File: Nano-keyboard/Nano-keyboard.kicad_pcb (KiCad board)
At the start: 2 copper layers, 120.1 x 80.2 mm, 39 parts, among them U1 QBC847BL, U2 ESP32-WROOM-32, U3 QBC847BL, U4 QBC847BL, U5 EN12-HN22AF25, U6 EN12-HN22AF25, U7 TP4050

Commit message: Minor changes
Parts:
- removed LED1, LED10, LED2, LED3, LED4, LED5, LED6, LED7, LED8, LED9: LRTBGVSR-U4V2-JW+A6BB-D8+S2U2-7Z-20-S, lib:LRTBGVSRU4V2JWA6BBD8S2U27Z20S
- removed U1, U3, U4: QBC847BL, lib:SOT96P237X111-3N
- D1, D10, D2, D3, D4, D5, D6, D7, D8, D9: footprint Diode_THT:D_DO-35_SOD27_P3.81mm_Vertical_AnodeUp -> Diode_THT:D_DO-35_SOD27_P7.62mm_Horizontal
- moved LED0 51.7 mm to (109.2, 69.8), turned to 90 degrees
- moved D1 3.83 mm to (106.9, 135.9)
- moved D2 3.83 mm to (124.9, 135.9)
- moved D3 3.83 mm to (142.9, 135.9)
- moved D4 3.83 mm to (160.8, 135.9)
- moved B0 3.83 mm to (98.7, 120.7)
- moved B1 3.83 mm to (117.7, 120.7)
- moved B2 3.83 mm to (135.7, 120.7)
- moved B3 3.83 mm to (153.7, 120.7)
- moved B4 3.83 mm to (171.6, 120.7)
- moved B6 1.91 mm to (135.5, 99.7)
- moved D5 1.91 mm to (106.7, 115.1)
- moved D6 1.91 mm to (124.4, 115.1)
- moved D7 1.91 mm to (142.7, 115.1)
- moved D8 1.91 mm to (160.9, 115.1)
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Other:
- board size 120.1 x 80.2 mm -> 113.3 x 77.2 mm

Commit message: Initial routing
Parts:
- removed U7: TP4050, lib:TP4050-module
- added U1: AMS1117, Package_TO_SOT_SMD:SOT-223-3_TabPin2, F.Cu at (72.4, 95.2)
- added U3: J5019, lib:J5019-module, F.Cu at (90.7, 100.4)
- moved B2 5.45 mm to (140.8, 118.7)
- moved B3 5.45 mm to (158.8, 118.7)
- moved B4 5.45 mm to (176.7, 118.7)
- moved B7 5.45 mm to (158.7, 97.8)
- moved B9 5.45 mm to (140.6, 76.8)
- moved B6 5.45 mm to (140.6, 97.8)
- moved D8 5.45 mm to (166.0, 113.2)
- moved B0 5.45 mm to (103.8, 118.7)
- moved B1 5.45 mm to (122.8, 118.7)
- moved B5 5.45 mm to (122.6, 97.8)
- moved D1 5.45 mm to (112.0, 134.0)
- moved U5 5.45 mm to (122.1, 75.2)
- moved B10 5.45 mm to (158.7, 76.8)
- moved B8 5.45 mm to (176.8, 97.8)
- moved D10 5.45 mm to (147.9, 92.1)
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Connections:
- LED0 pad A1: /ANODE_G -> /LED_GREEN
- LED0 pad A2: /ANODE_R -> /LED_RED
- LED0 pad A3: /ANODE_B -> /LED_BLUE
- U2 pad 16: unconnected-(U2-Pad16) -> ROW1
- U2 pad 23: unconnected-(U2-Pad23) -> ROW2
- U2 pad 24: unconnected-(U2-Pad24) -> ROW3
- U2 pad 30: unconnected-(U2-Pad30) -> /FUNC
- U2 pad 31: unconnected-(U2-Pad31) -> COL1
- U2 pad 33: unconnected-(U2-Pad33) -> COL2
- U2 pad 36: unconnected-(U2-Pad36) -> COL3
- U2 pad 37: unconnected-(U2-Pad37) -> COL4
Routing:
- net ROW1: track 0.00 -> 128.3 mm
- net COL4: track 0.00 -> 105.2 mm
- net COL2: track 0.00 -> 96.2 mm
- net ROW2: track 0.00 -> 92.3 mm
- net COL3: track 0.00 -> 86.6 mm
- net COL1: track 0.00 -> 79.3 mm
- net /FUNC: track 0.00 -> 45.7 mm, vias 0 -> 1
- net ROW3: track 0.00 -> 36.4 mm, vias 0 -> 2
- net Net-(B6-Pad1): track 0.00 -> 16.8 mm
- net Net-(B7-Pad1): track 0.00 -> 16.8 mm
- net Net-(B9-Pad1): track 0.00 -> 16.7 mm
- net Net-(B5-Pad1): track 0.00 -> 16.7 mm
- net Net-(B8-Pad1): track 0.00 -> 16.7 mm
- net Net-(B10-Pad1): track 0.00 -> 16.6 mm
- net Net-(B4-Pad1): track 0.00 -> 16.6 mm
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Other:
- board size 113.3 x 77.2 mm -> 118.3 x 77.2 mm

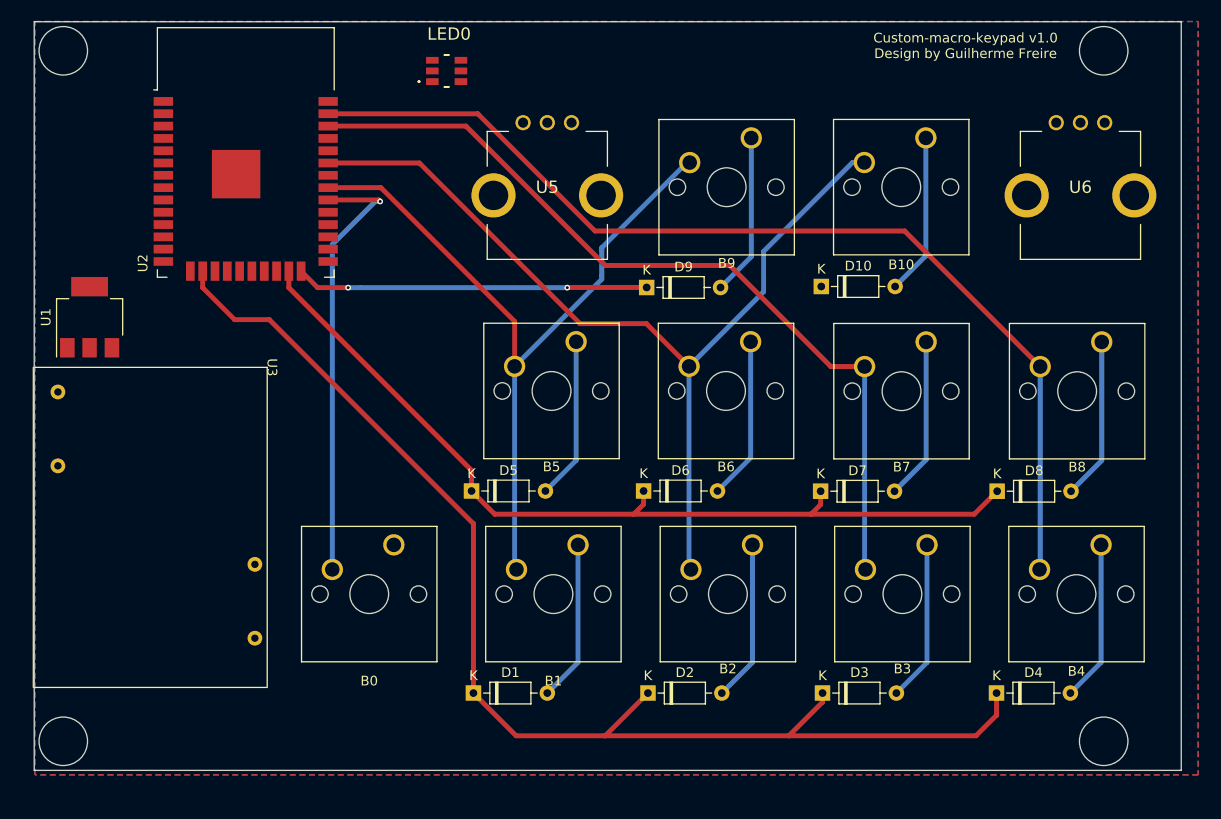
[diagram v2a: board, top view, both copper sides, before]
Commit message: Added Resistors and Capacitor
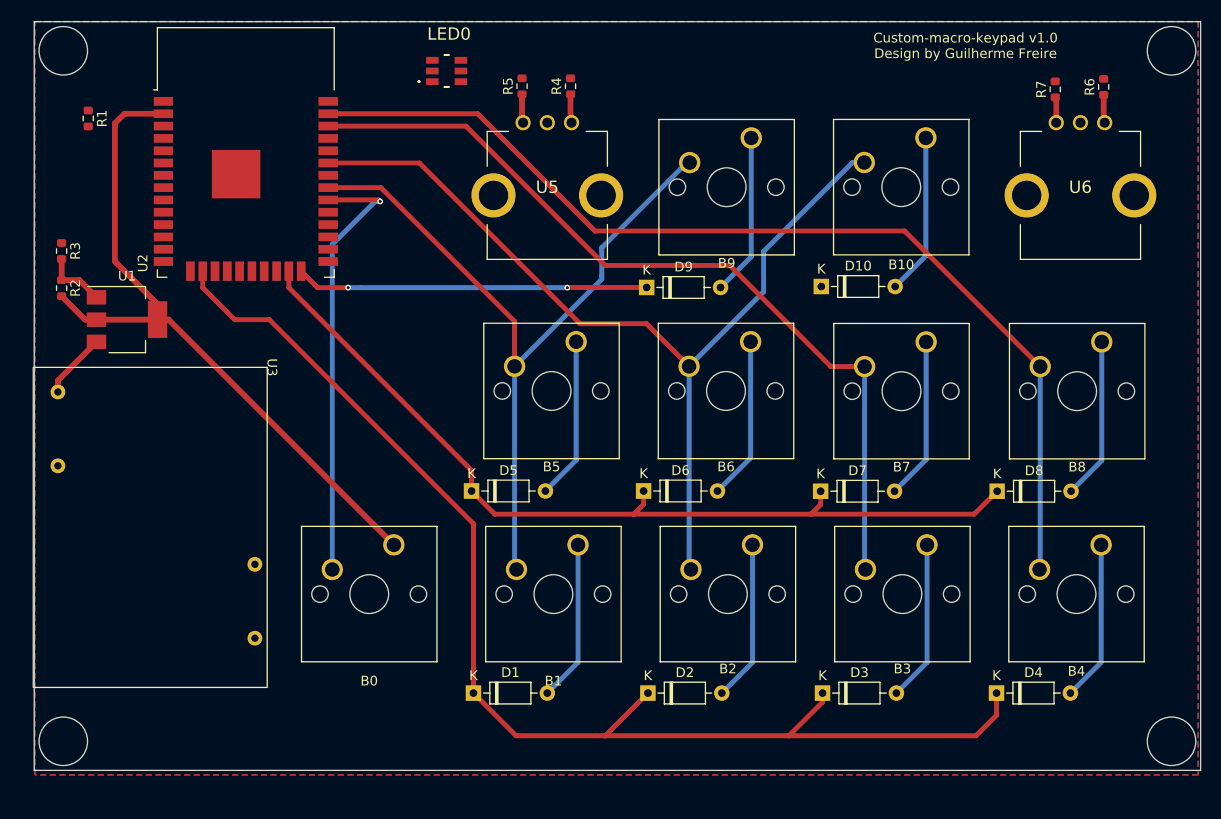
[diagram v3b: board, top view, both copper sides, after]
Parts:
- added R1: R_0603, lib:R_0603_1608Metric, F.Cu at (72.2, 74.8)
- added R2: 600R, lib:R_0603_1608Metric, F.Cu at (69.5, 92.2)
- added R3: 1kR, lib:R_0603_1608Metric, F.Cu at (69.5, 88.4)
- added R4: R_0603, lib:R_0603_1608Metric, F.Cu at (122.0, 71.4)
- added R5: R_0603, lib:R_0603_1608Metric, F.Cu at (117.0, 71.4)
- added R6: R_0603, lib:R_0603_1608Metric, F.Cu at (177.0, 71.5)
- added R7: R_0603, lib:R_0603_1608Metric, F.Cu at (172.0, 71.8)
- moved U1 3.87 mm to (76.2, 95.5), turned to 0 degrees
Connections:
- U1 pad 1: unconnected-(U1-Pad1) -> Net-(U1-Pad1)
- U2 pad 11: unconnected-(U2-Pad11) -> /ENCODER1_A
- U2 pad 12: unconnected-(U2-Pad12) -> /ENCODER1_B
- U2 pad 13: unconnected-(U2-Pad13) -> /ENCODER2_A
- U2 pad 14: unconnected-(U2-Pad14) -> /ENCODER2_B
- U2 pad 3: unconnected-(U2-Pad3) -> /ESP_EN
- U5 pad A1: unconnected-(U5-PadA1) -> /ENCODER2_A
- U5 pad B1: unconnected-(U5-PadB1) -> /ENCODER2_B
- U5 pad C1: Net-(U5-PadC1) -> GND
- U6 pad A1: unconnected-(U6-PadA1) -> /ENCODER1_A
- U6 pad B1: unconnected-(U6-PadB1) -> /ENCODER1_B
- U6 pad C1: Net-(U5-PadC1) -> GND
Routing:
- net +3V3: track 0.00 -> 72.6 mm
- net Net-(U1-Pad3): track 0.00 -> 6.81 mm
- net Net-(U1-Pad1): track 0.00 -> 6.51 mm
- net /ENCODER2_B: track 0.00 -> 2.98 mm
- net /ENCODER2_A: track 0.00 -> 2.98 mm
- net /ENCODER1_A: track 0.00 -> 2.90 mm
- net /ENCODER1_B: track 0.00 -> 2.65 mm
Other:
- board size 118.3 x 77.2 mm -> 120.3 x 77.2 mm

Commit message: Routing changes
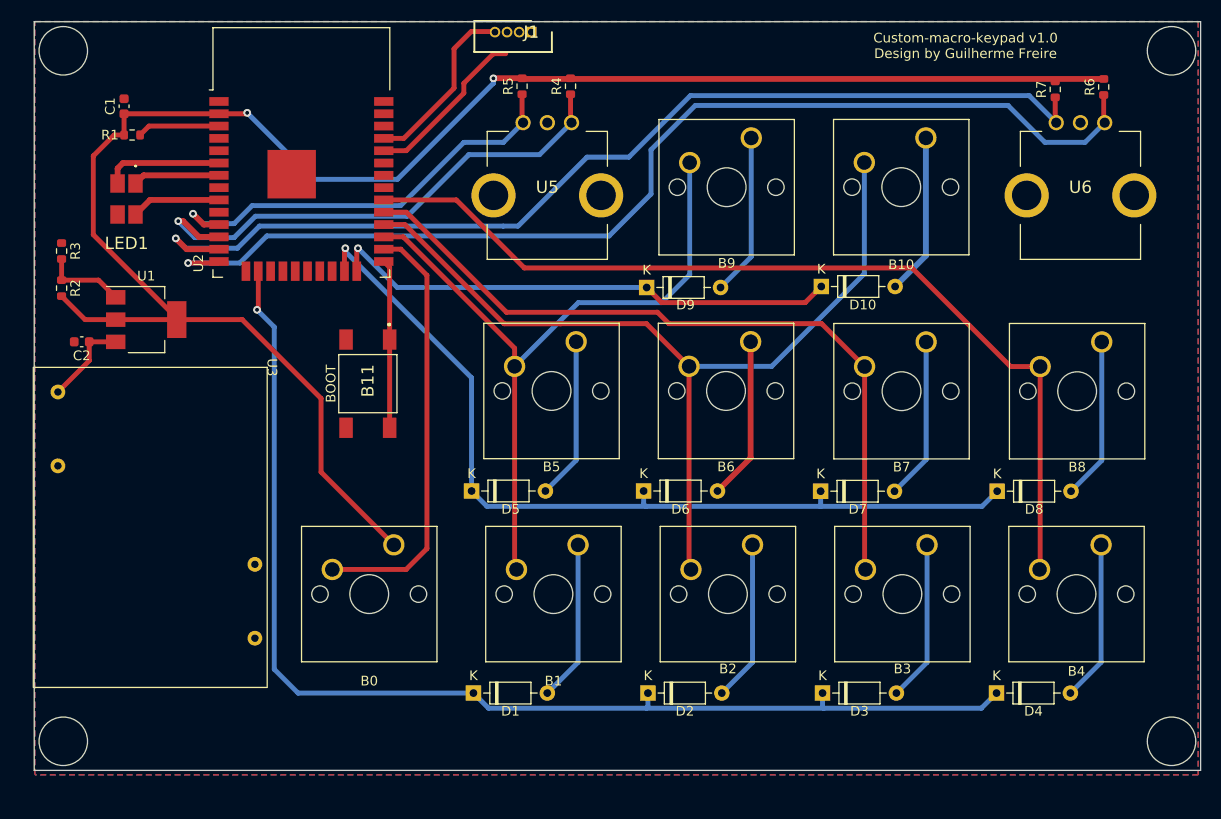
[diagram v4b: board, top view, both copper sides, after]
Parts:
- removed LED0: LRTBGVSR-U4V2-JW+A6BB-D8+S2U2-7Z-20-S, lib:LRTBGVSRU4V2JWA6BBD8S2U27Z20S
- added B11: LL3301NF065QG, lib:LL3301NF065QG, F.Cu at (101.1, 102.1)
- added C1: C_0603, lib:C_0603_1608Metric, F.Cu at (75.9, 73.5)
- added C2: C_0603, lib:C_0603_1608Metric, F.Cu at (71.6, 97.8)
- added J1: 125SH-B-04-TS, lib:SHDR4W35P0X125_1X4_800X320X420P, F.Cu at (118.0, 65.8)
- added LED1: 598-8610-307F, lib:5988610307F, F.Cu at (76.2, 83.1)
- R2: value 600R -> R_0603
- R3: value 1kR -> R_0603
- moved U2 5.73 mm to (94.2, 81.2)
- moved R1 4.83 mm to (76.8, 76.5), turned to 0 degrees
- moved U1 1.98 mm to (78.2, 95.5)
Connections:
- U2 pad 11: /ENCODER1_A -> /ENCODER2_B
- U2 pad 12: /ENCODER1_B -> /ENCODER2_A
- U2 pad 13: /ENCODER2_A -> /ENCODER1_B
- U2 pad 14: /ENCODER2_B -> /ENCODER1_A
- U2 pad 26: unconnected-(U2-Pad26) -> /FUNC
- U2 pad 27: unconnected-(U2-Pad27) -> COL1
- U2 pad 28: unconnected-(U2-Pad28) -> COL2
- U2 pad 29: unconnected-(U2-Pad29) -> COL3
- U2 pad 30: /FUNC -> COL4
- U2 pad 31: COL1 -> unconnected-(U2-Pad31)
- U2 pad 33: COL2 -> unconnected-(U2-Pad33)
- U2 pad 34: unconnected-(U2-Pad34) -> /RX0
- U2 pad 35: unconnected-(U2-Pad35) -> /TX0
- U2 pad 36: COL3 -> unconnected-(U2-Pad36)
- U2 pad 37: COL4 -> unconnected-(U2-Pad37)
- U2 pad 6: /LED_GREEN -> /LED_BLUE
- U2 pad 7: /LED_BLUE -> /LED_GREEN
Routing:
- net +3V3: track 72.6 -> 184.6 mm, vias 0 -> 2
- net /ENCODER1_A: track 2.90 -> 112.5 mm, vias 0 -> 1
- net /ENCODER1_B: track 2.65 -> 106.5 mm, vias 0 -> 1
- net /ENCODER2_A: track 2.98 -> 54.0 mm, vias 0 -> 1
- net /ENCODER2_B: track 2.98 -> 44.9 mm, vias 0 -> 1
- net /TX0: track 0.00 -> 18.5 mm
- net /BOOT: track 0.00 -> 17.4 mm
- net /RX0: track 0.00 -> 17.3 mm
- net ROW3: track 36.4 -> 53.2 mm, vias 2 -> 1
- net /LED_BLUE: track 0.00 -> 12.2 mm
- net COL4: track 105.2 -> 95.8 mm
- net COL3: track 86.6 -> 77.2 mm
- net /LED_RED: track 0.00 -> 9.23 mm
- net /LED_GREEN: track 0.00 -> 8.96 mm
- net /ESP_EN: track 0.00 -> 8.52 mm
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
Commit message: Routing Done [Pending Revision]
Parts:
- added J2: 125SH-B-02-TS, lib:125SHB02TS, F.Cu at (80.5, 140.1)
- added R8: R_0603, lib:R_0603_1608Metric, F.Cu at (76.1, 88.1)
- moved J1 0.99 mm to (117.1, 66.4)
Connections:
- LED1 pad 4: GND -> Net-(LED1-Pad4)
- U3 pad 1: unconnected-(U3-Pad1) -> Net-(U3-Pad1)
- U3 pad 2: unconnected-(U3-Pad2) -> Net-(U3-Pad2)
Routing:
- net Net-(U3-Pad1): track 0.00 -> 25.5 mm
- net Net-(U3-Pad2): track 0.00 -> 16.7 mm
- net Net-(LED1-Pad4): track 0.00 -> 3.41 mm
- net /TX0: track 18.5 -> 17.3 mm
- net /RX0: track 17.3 -> 18.0 mm
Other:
- board text added: "Nano-Keyboard v1.1 Design by Guilherme Freire"
- board text removed: "Custom-macro-keypad v1.0 Design by Guilherme Freire"

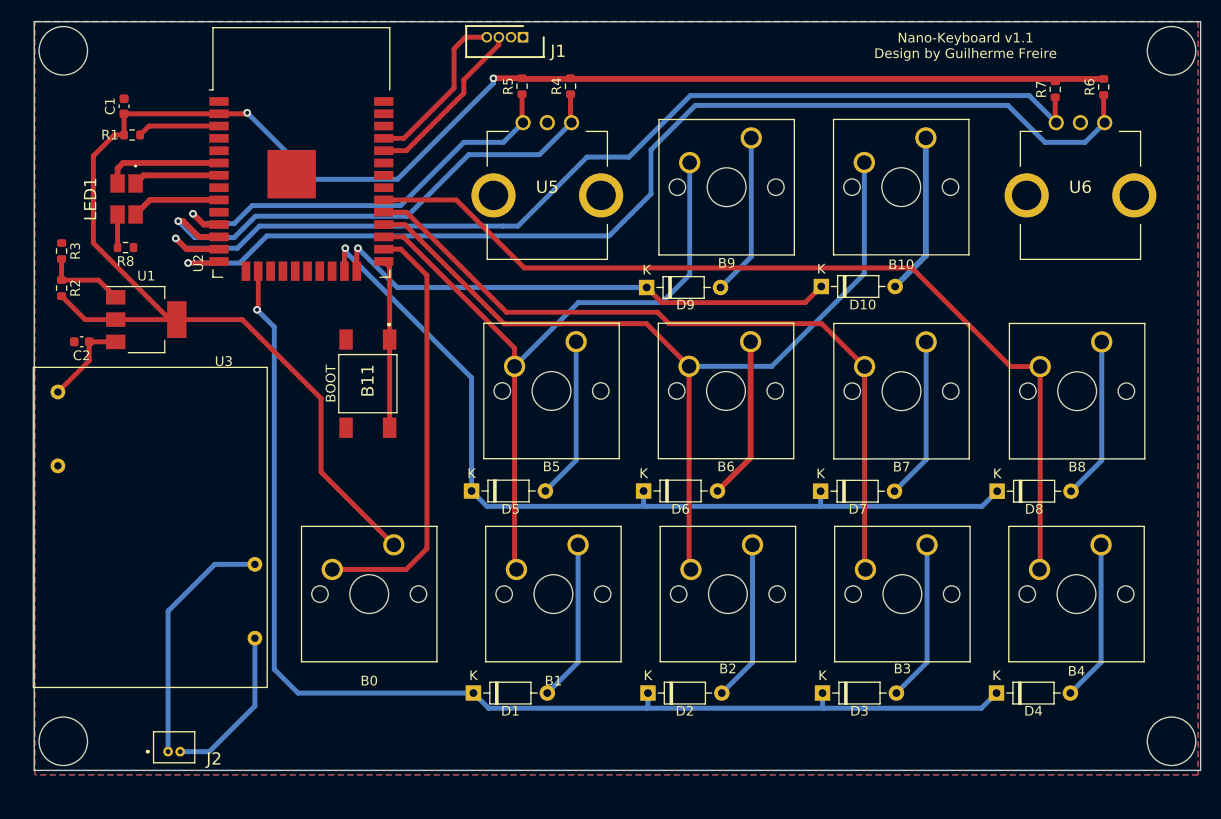
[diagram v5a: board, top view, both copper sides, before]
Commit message: Added RGB leds
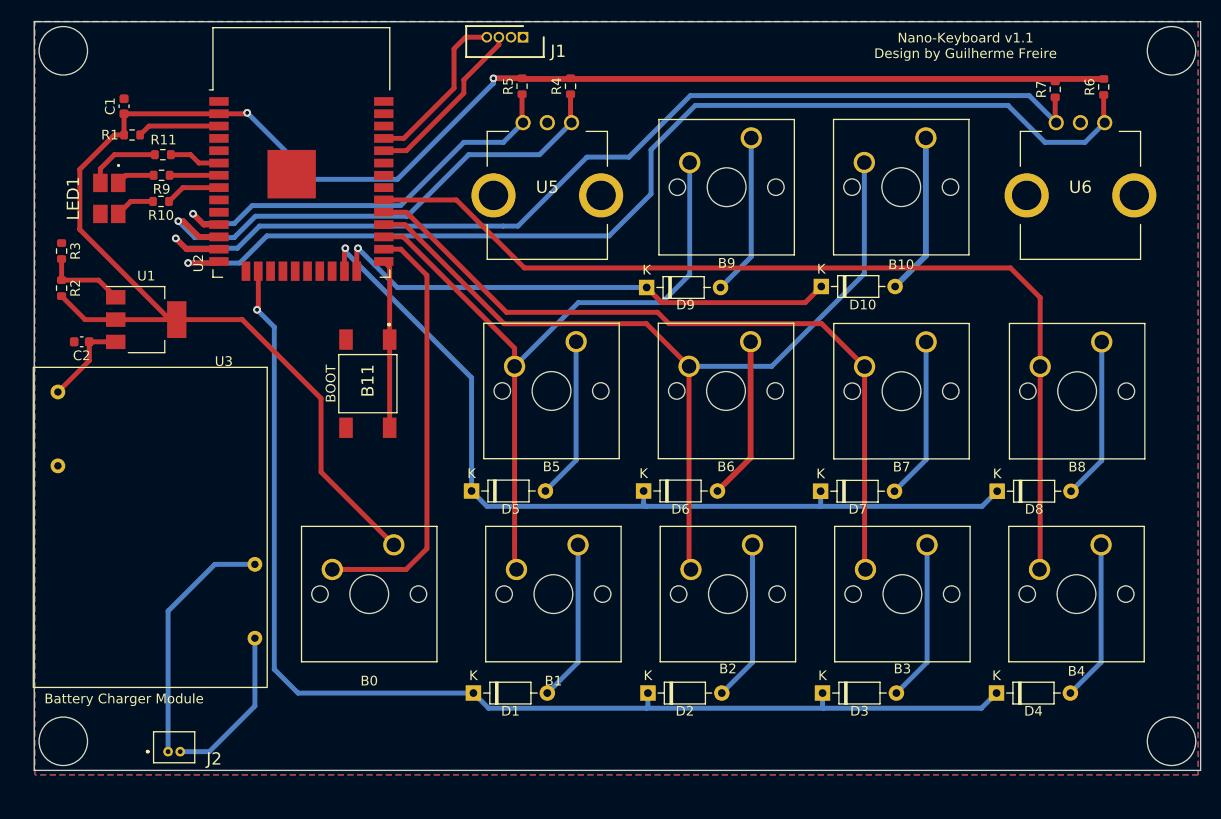
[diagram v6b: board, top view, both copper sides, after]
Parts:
- removed R8: R_0603, lib:R_0603_1608Metric
- added R10: R_0603, lib:R_0603_1608Metric, F.Cu at (79.8, 83.3)
- added R11: R_0603, lib:R_0603_1608Metric, F.Cu at (79.9, 78.5)
- added R9: R_0603, lib:R_0603_1608Metric, F.Cu at (79.8, 80.6)
- moved LED1 1.78 mm to (74.4, 83.0)
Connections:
- LED1 pad 1: /LED_GREEN -> Net-(LED1-Pad1)
- LED1 pad 2: /LED_RED -> Net-(LED1-Pad2)
- LED1 pad 3: /LED_BLUE -> Net-(LED1-Pad3)
- LED1 pad 4: Net-(LED1-Pad4) -> GND
- U2 pad 8: unconnected-(U2-Pad8) -> /LED_RED
- U2 pad 9: /LED_RED -> unconnected-(U2-Pad9)
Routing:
- net Net-(LED1-Pad3): track 0.00 -> 7.69 mm
- net /LED_BLUE: track 12.2 -> 5.32 mm
- net COL4: track 95.8 -> 100.0 mm
- net Net-(LED1-Pad2): track 0.00 -> 4.12 mm
- net Net-(LED1-Pad1): track 0.00 -> 3.97 mm
- net /LED_GREEN: track 8.96 -> 5.09 mm
- net /LED_RED: track 9.23 -> 5.74 mm
- net Net-(LED1-Pad4): track 3.41 -> 0.00 mm
- net +3V3: track 185.1 -> 186.2 mm
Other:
- board text added: "Battery Charger Module"

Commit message: Board Dimensions changes
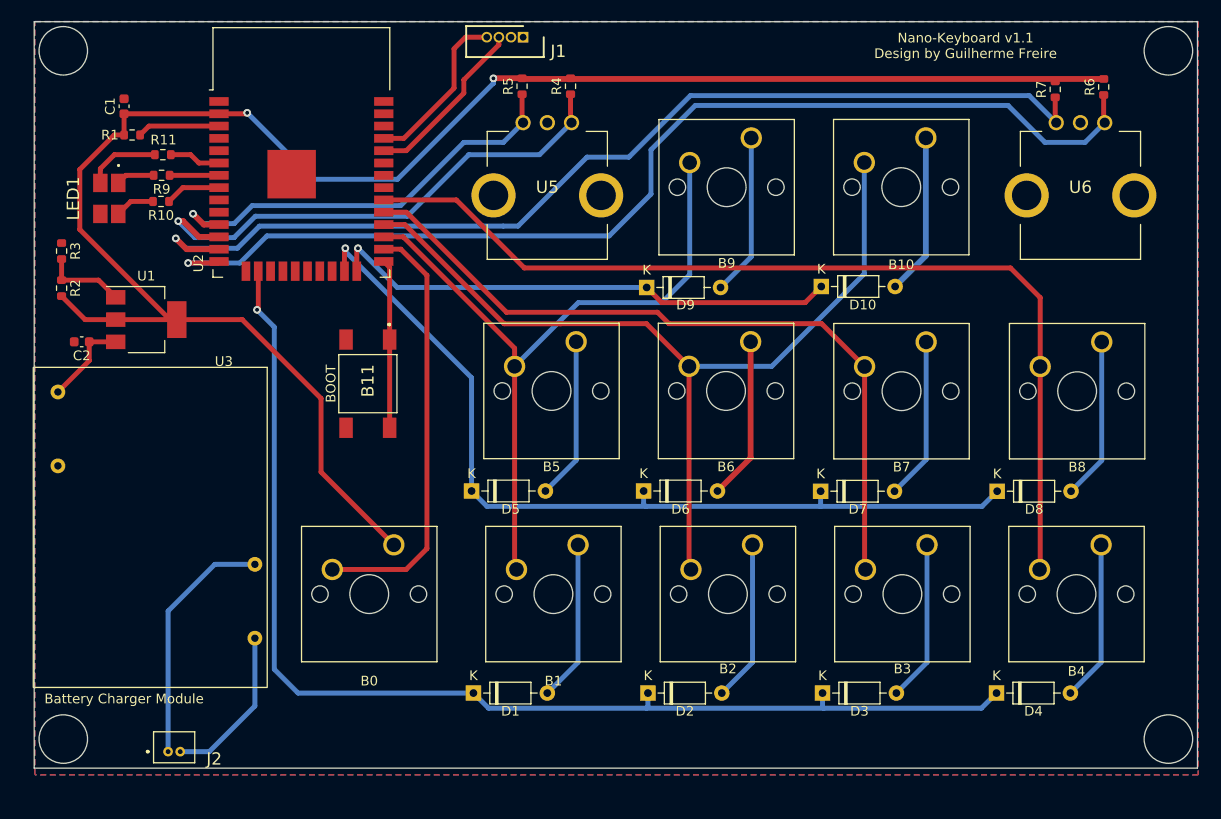
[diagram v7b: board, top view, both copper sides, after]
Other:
- board size 120.3 x 77.2 mm -> 120 x 77 mm
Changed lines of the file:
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@@
     )
   )
-  (gr_circle locked (center 184 67.77) (end 186.5 67.77) (layer "Edge.Cuts") (width 0.1) (fill none))
-  (gr_circle locked (center 184 139) (end 186.5 139) (layer "Edge.Cuts") (width 0.1) (fill none))
+  (gr_circle locked (center 183.675 67.77) (end 186.175 67.77) (layer "Edge.Cuts") (width 0.1) (fill none))
+  (gr_circle locked (center 183.675 138.77) (end 186.175 138.77) (layer "Edge.Cuts") (width 0.1) (fill none))
   (gr_circle locked (center 69.675 67.77) (end 72.175 67.77) (layer "Edge.Cuts") (width 0.1) (fill none))
-  (gr_circle locked (center 69.675 139) (end 72.175 139) (layer "Edge.Cuts") (width 0.1) (fill none))
-  (gr_rect locked (start 66.675 64.77) (end 187 142) (layer "Edge.Cuts") (width 0.1) (fill none))
+  (gr_circle locked (center 69.675 138.77) (end 72.175 138.77) (layer "Edge.Cuts") (width 0.1) (fill none))
+  (gr_rect locked (start 66.675 64.77) (end 186.675 141.77) (layer "Edge.Cuts") (width 0.1) (fill none))
   (gr_text "github.com/Freireg/Custom-Macro-Keypad" (at 163.068 139.192) (layer "B.SilkS")
     (effects (font (size 1 1) (thickness 0.15)) (justify mirror))
@@
   )
   (dimension (type aligned) (layer "Dwgs.User")
-    (pts (xy 66.675 64.77) (xy 187 64.77))
+    (pts (xy 66.675 64.77) (xy 186.675 64.77))
     (height -9.525)
-    (gr_text "120,3250 mm" (at 126.8375 54.095) (layer "Dwgs.User")
+    (gr_text "120,0000 mm" (at 126.675 54.095) (layer "Dwgs.User")
       (effects (font (size 1 1) (thickness 0.15)))
     )
@@
   )
   (dimension (type aligned) (layer "Dwgs.User")
-    (pts (xy 66.675 64.77) (xy 66.675 142))
+    (pts (xy 66.675 64.77) (xy 66.675 141.77))
     (height 10.795)
-    (gr_text "77,2300 mm" (at 54.08 103.385 90) (layer "Dwgs.User")
+    (gr_text "77,0000 mm" (at 54.08 103.27 90) (layer "Dwgs.User")
       (effects (font (size 1.5 1.5) (thickness 0.3)))
     )
